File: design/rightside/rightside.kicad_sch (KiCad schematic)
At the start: 159 parts, among them IC2 XC9148G50CER-G, IC3 nRF52833-QDAA-R7, IC4 74AHCT125PW,118, IC5 MCP23018T-E_SS, IC6 XC9291B33D1R-G, J1 USB_C_Receptacle_USB2.0_16P, J2 Battery Pos, J3 Battery Neg, J4 OLED_128x32, J5 SFV12R-1STBE1HLF, J6 Conn_01x04, U2 BQ24072RGT, U3 USB6B1, U4 BQ27441-G1, U5 PEC11L-4015F-S0015, U6 PEC11L-4015F-S0015, X1 32MHz

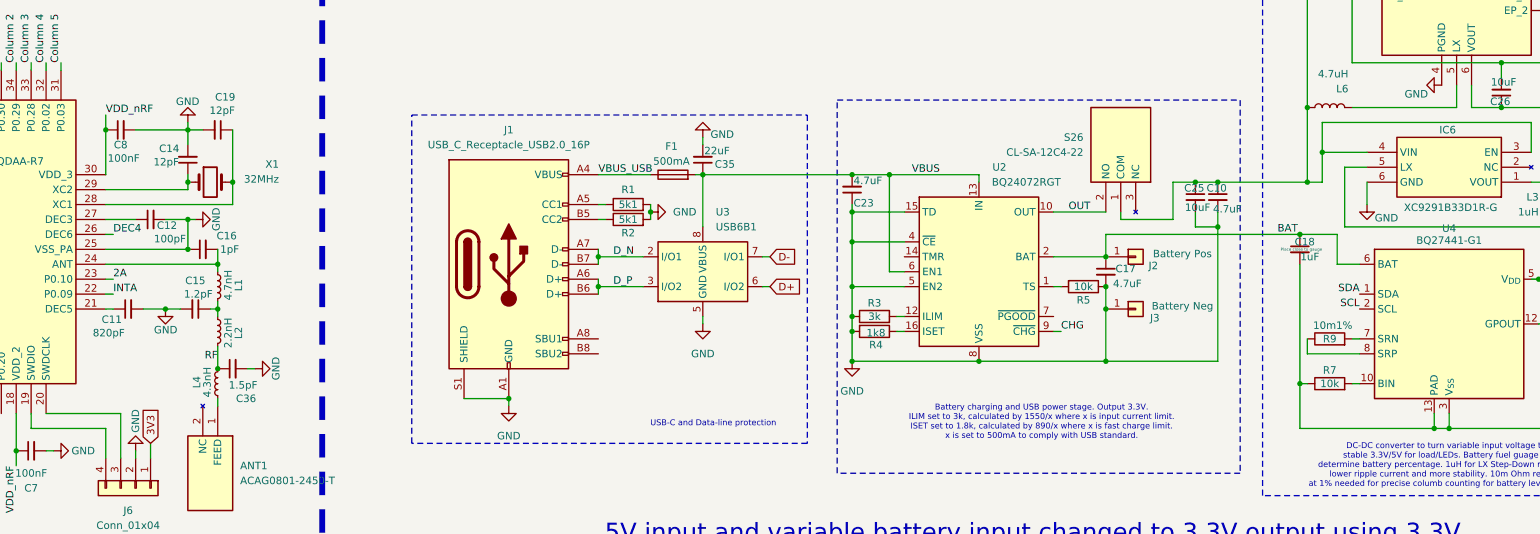
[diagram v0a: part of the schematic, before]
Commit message: correct fuel gauge and crystal
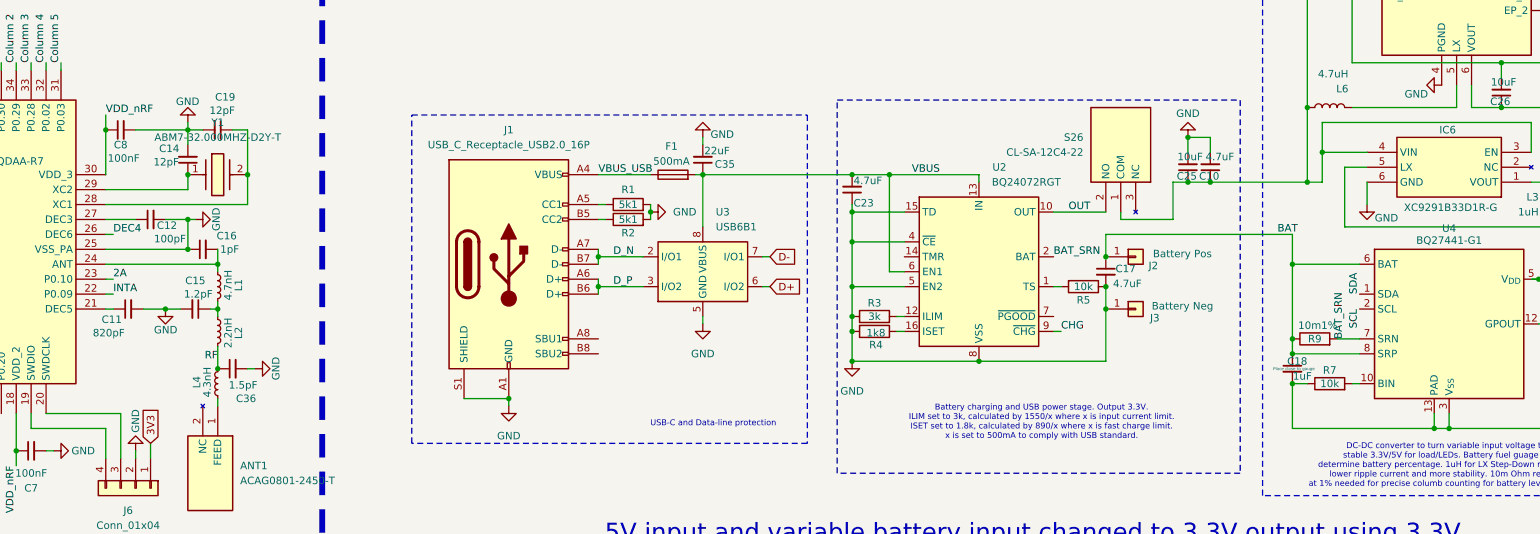
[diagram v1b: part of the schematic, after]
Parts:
- removed X1: 32MHz, Crystal:Crystal_SMD_ECS_CSM3X-2Pin_7.6x4.1mm, symbol Device:Crystal
- added Y1: ABM7-32.000MHZ-D2Y-T, ABM7, symbol SamacSys_Parts:ABM7-32.000MHZ-D2Y-T
- J6: footprint (none) -> Connector_PinHeader_2.54mm:PinHeader_1x04_P2.54mm_Horizontal
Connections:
- net BAT: now also R9.1, U4.8 (SRP); no longer U2.2 (BAT), U2.3 (BAT)
- net BAT_SRN: now reaches R9.2, U4.7 (SRN)
- net BAT_SRN: now also U2.2 (BAT), U2.3 (BAT)
- net at C14.1, IC3.29 (XC2): now also Y1.1
- net at C19.1, IC3.28 (XC1): now also Y1.2
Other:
- moved on the sheet: C10, C18, C25, R9

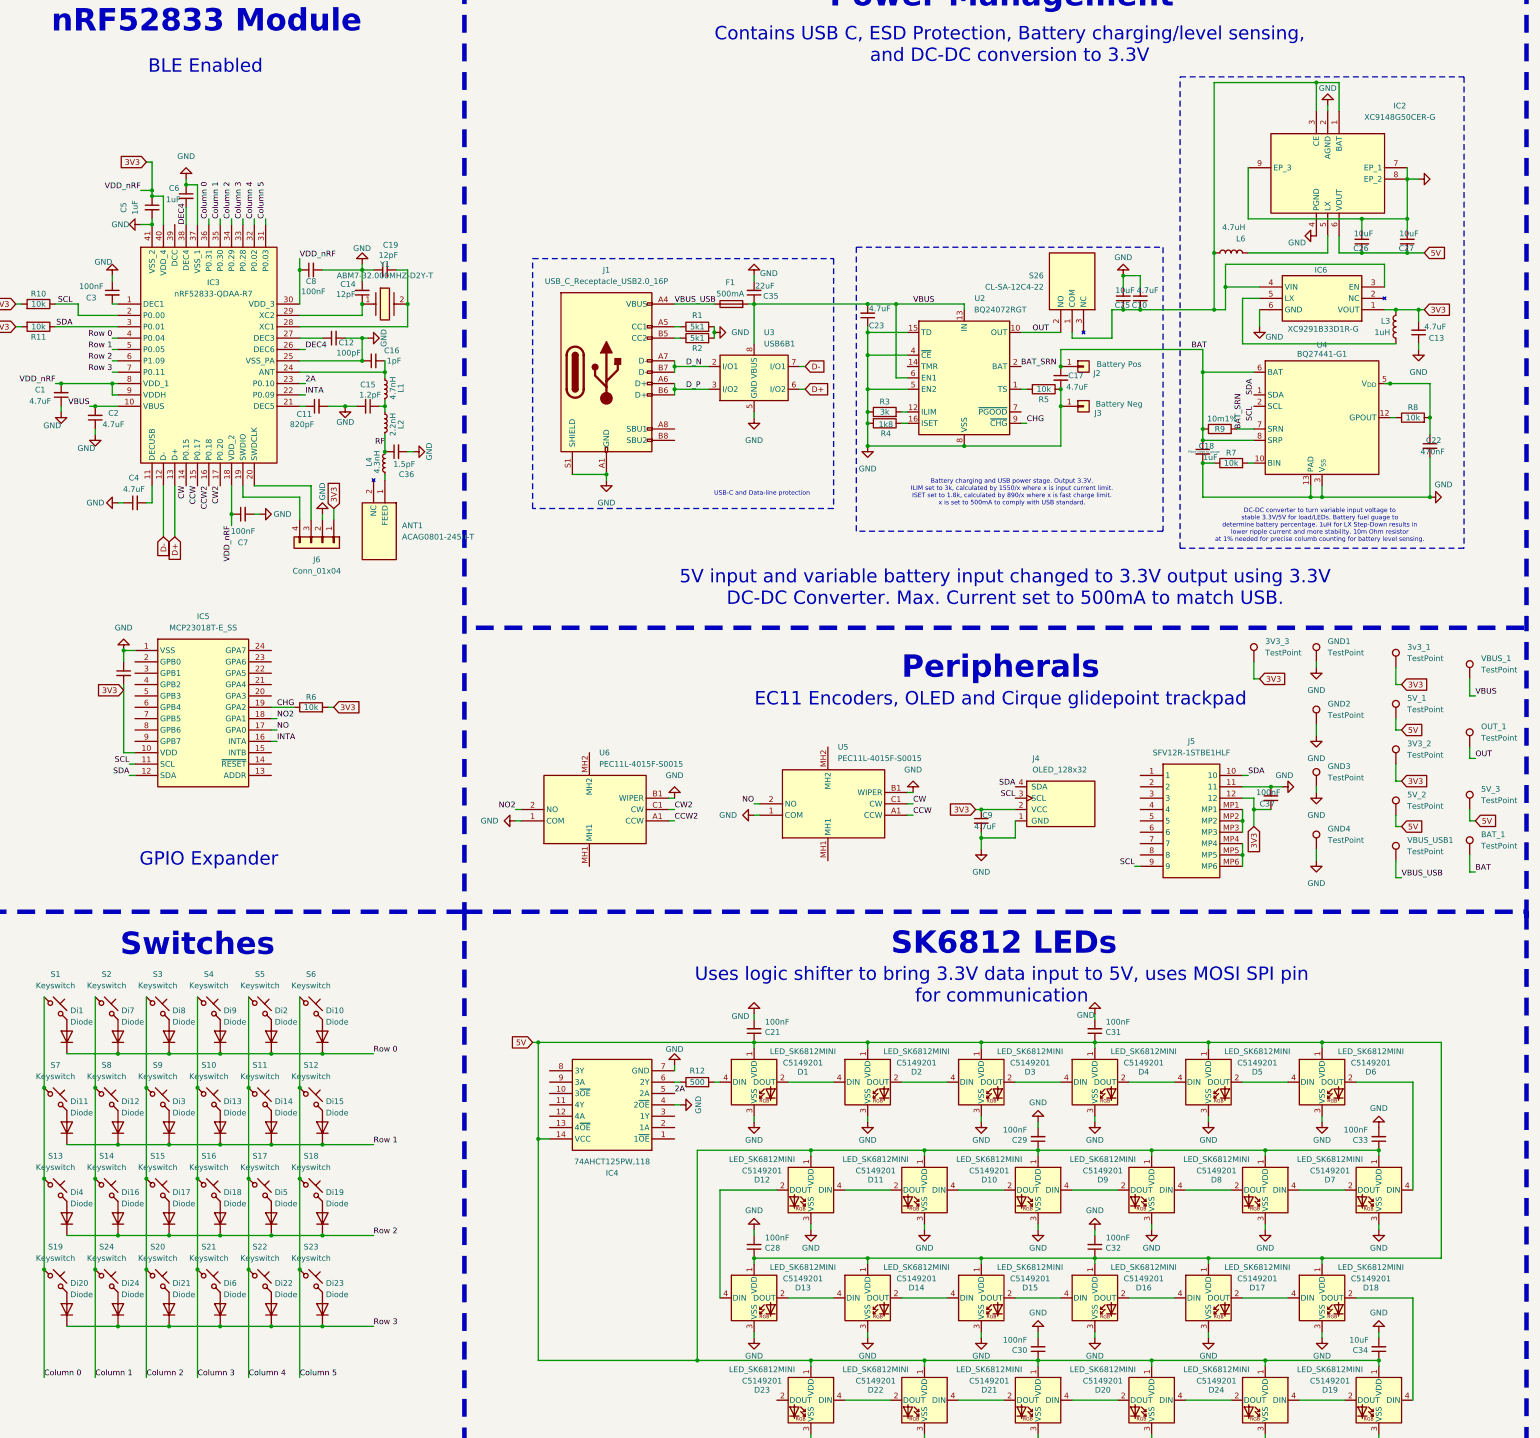
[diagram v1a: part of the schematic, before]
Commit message: prepare to reroute
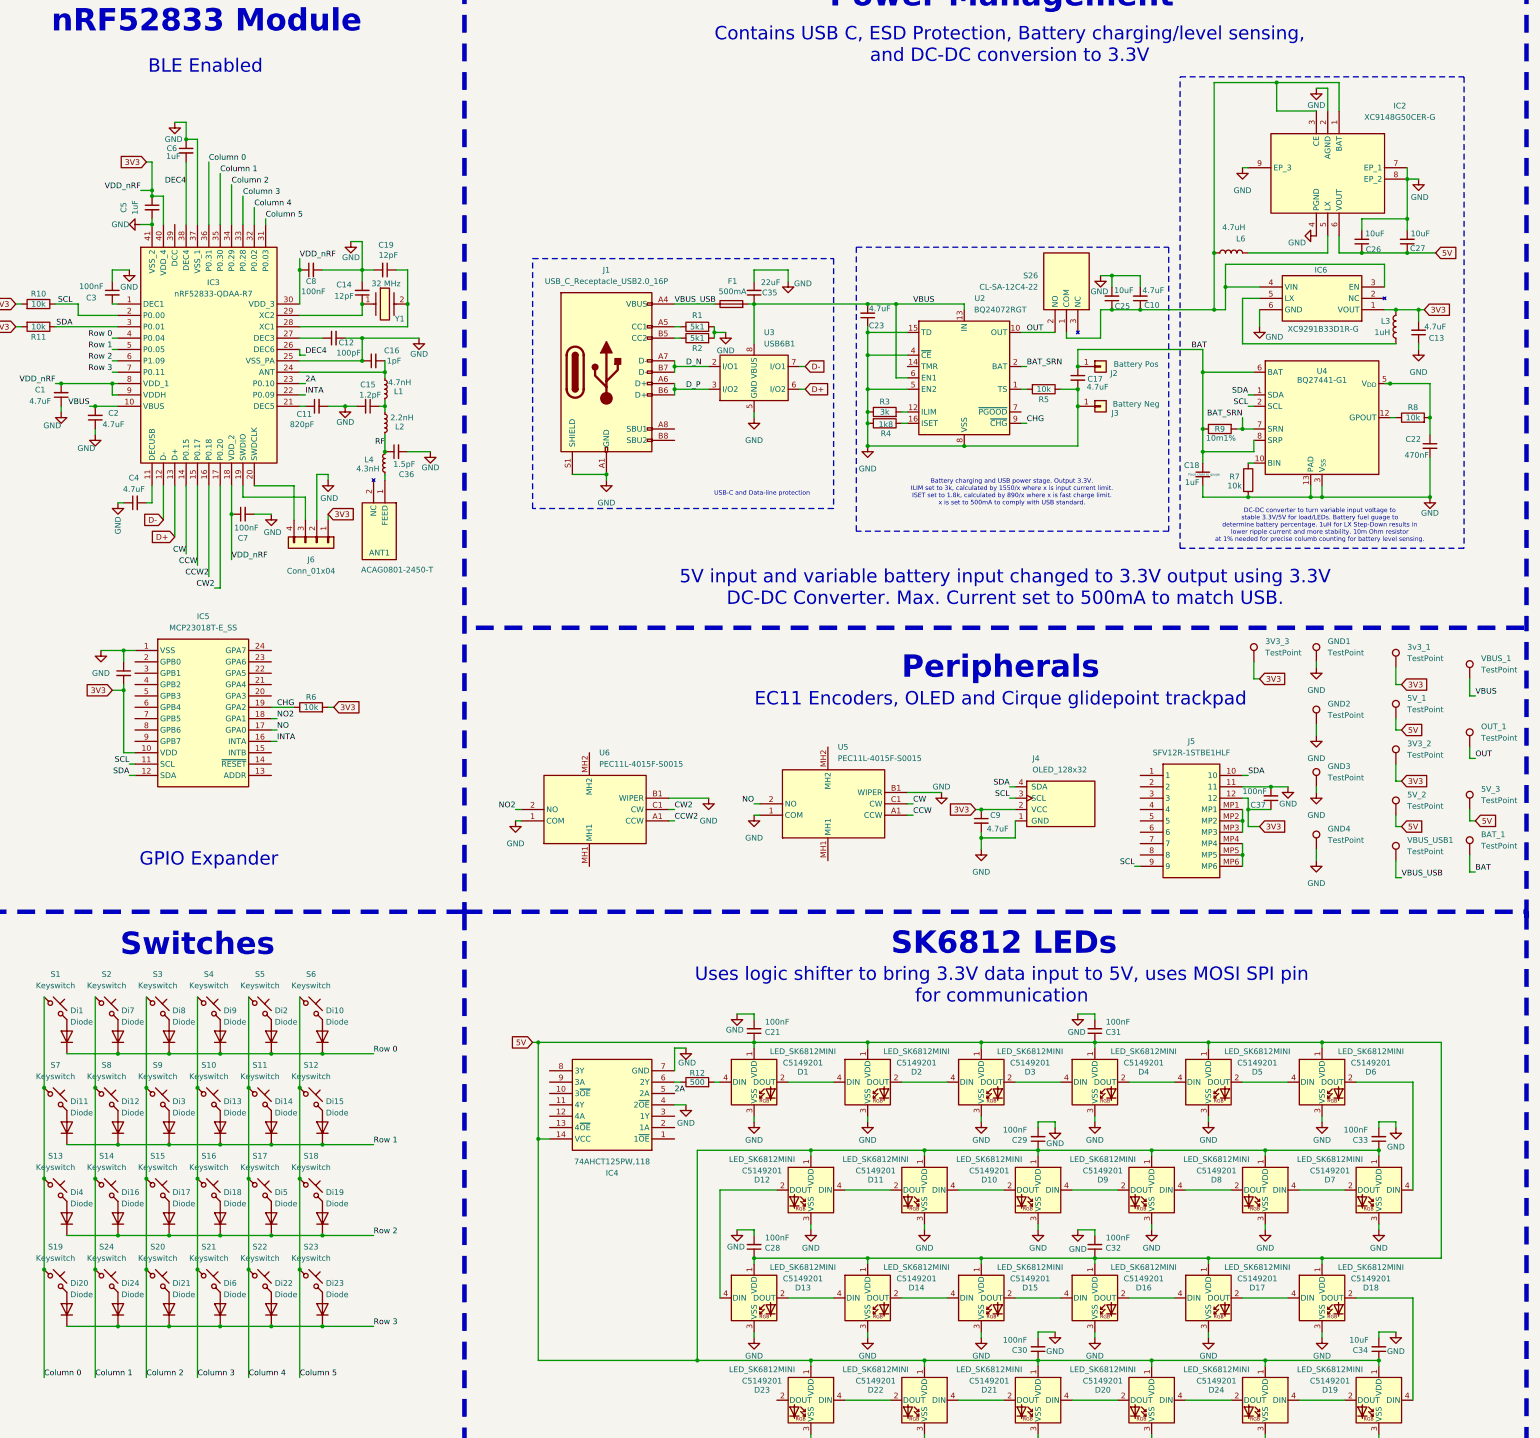
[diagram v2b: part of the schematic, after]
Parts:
- Y1: value ABM7-32.000MHZ-D2Y-T -> 32 MHz
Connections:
- net GND: now also R7.2; no longer R7.1
- net at U4.10 (BIN): now also R7.1; no longer R7.2
- net at IC3.19 (SWDIO): now also J6.3 (Pin_3); no longer J6.4 (Pin_4)
- net at IC3.20 (SWDCLK): now also J6.4 (Pin_4); no longer J6.3 (Pin_3)
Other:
- moved on the sheet: C17, C18, C25, C6, J2, J3, J6, R7, S26

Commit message: prepare to make test board
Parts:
- removed L4: 4.3nH, Inductor_SMD:L_0603_1608Metric, symbol Device:L_Small
- removed R10, R11, R6: 10k, Resistor_SMD:R_0603_1608Metric, symbol Device:R
- added C24: 4.7uF, ScottoKeebs_Components:Capacitor_0603, symbol Device:C_Small
- added C38, C39, C40: 100nF, ScottoKeebs_Components:Capacitor_0603, symbol Device:C_Small
- C35: value 22uF -> 100nF
- C36: value 1.5pF -> 100nF
- F1: value 500mA -> 600mA
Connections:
- net 3V3: now also C35.2, C36.2, C38.2, C39.2, C40.2
- net GND: now also C35.1, C36.1, C24.2, C38.1, C39.1, C40.1; no longer C35.2, C36.2
- net RF: now also ANT1.1 (FEED); no longer C36.1
- net VBUS: now also C24.1; no longer C35.1
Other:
- note added: "Stitching Capacitors"
- note added: "Test Points"
- moved on the sheet: 3V3_2, 3V3_3, 3v3_1, 5V_1, 5V_2, 5V_3, ANT1, BAT_1, C21, C28, C29, C30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

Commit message: remove old right side routing
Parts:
- removed C35, C36, C38, C39: 100nF, ScottoKeebs_Components:Capacitor_0603, symbol Device:C_Small
- removed J5: SFV12R-1STBE1HLF, SFV12R1STBE1HLF, symbol SamacSys_Parts:SFV12R-1STBE1HLF
- removed L6: 4.7uH, Inductor_SMD:L_0603_1608Metric, symbol Device:L
- removed R12: 500, Resistor_SMD:R_0603_1608Metric, symbol Device:R
- removed Y1: 32 MHz, ABM7, symbol SamacSys_Parts:ABM7-32.000MHZ-D2Y-T
- added J7: F32Q-1A7H1-11012, F32Q1A7H111012, symbol SamacSys_Parts:F32Q-1A7H1-11012
- added L4: SRN3015C-4R7M, SRN3015C4R7M, symbol SamacSys_Parts:SRN3015C-4R7M
- added R10: 3k, Resistor_SMD:R_0603_1608Metric, symbol Device:R
- added R6: 10m1%, RESC2012X41N, symbol SamacSys_Parts:TLR2ATTD10L0F
- added Y1: ECS-320-8-37B2-JTY-TR, ECS320837B2JTYTR, symbol SamacSys_Parts:ECS-320-8-37B2-JTY-TR
- C26, C27: value 10uF -> 10uF-lowESR
- R9: value 10m1% -> 10k
- renumbered 3V3_3 to 5V_4
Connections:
- net 3V3: now also R9.2, J7.12; no longer 5V_4.1
- net 5V: now also 5V_4.1
- net BAT: now also R6.1; no longer R9.1
- net BAT_SRN: now also R6.2; no longer R9.2
- net GND: now also IC4.1 (1~{OE}), IC4.10 (3~{OE}), IC4.13 (4~{OE}), IC5.13 (ADDR), J7.11, Y1.2 (GND_1), Y1.4 (GND_2)
- net SCL: now also J7.9
- net SDA: now also J7.10
- net at C10.1, C25.1, IC2.1 (BAT)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: now also L4.1
- net at D20.4 (DIN): now also D19.2 (DOUT); no longer D24.2 (DOUT)
- net at D24.4 (DIN): now also D23.2 (DOUT); no longer D19.2 (DOUT)
- net at C14.1, IC3.29 (XC2): now also Y1.1 (IN/OUT)
- net at C19.1, IC3.28 (XC1): now also Y1.3 (OUT/IN)
- net at D1.4 (DIN): now also R10.2
- net at IC2.5 (LX): now also L4.2
- net at IC5.14 (~{RESET}): now also R9.1
- net at IC4.6 (2Y): now also R10.1
- net DEC4 renamed DEC4_6
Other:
- moved on the sheet: C14, C18, C19, C22, C37, C40, D20, D21, D22, D23, D24, J6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

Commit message: restructure for right side and add correct mounting holes
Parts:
- removed OUT_1: TestPoint, TestPoint:TestPoint_Pad_D1.5mm, symbol Connector:TestPoint
- removed U4: BQ27441-G1, Package_SON:Texas_S-PDSO-N12, symbol Battery_Management:BQ27441-G1
- added 5V_5: TestPoint, TestPoint:TestPoint_Pad_D1.5mm, symbol Connector:TestPoint
- added C35, C36, C38, C39, C41, C42, C43, C45, C46: 100nF, ScottoKeebs_Components:Capacitor_0603, symbol Device:C_Small
- added C44: 10uF, ScottoKeebs_Components:Capacitor_0603, symbol Device:C_Small
- added D25, D26, D27, D28, D29, D30, D31, D32, D33, D34, D35, D36, D37, D38, D39, D40, D41, D42, D43, D44, D45, D46, D47, D48: LED_SK6812MINI, ScottoKeebs_Components:LED_SK6812MINI, symbol ScottoKeebs:LED_SK6812MINI
- added U1: BQ27441-G1, Package_SON:Texas_S-PDSO-N12, symbol Battery_Management:BQ27441-G1
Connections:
- net 3V3: no longer C40.2
- net 5V: now also C40.2, 5V_5.1, C35.1, C36.1, C38.1, C39.1, C41.1, C42.1, C43.1, C44.1, C45.1, C46.2, D25.1 (VDD), D26.1 (VDD), D27.1 (VDD), D28.1 (VDD), D29.1 (VDD), D30.1 (VDD), D31.1 (VDD), D32.1 (VDD), D33.1 (VDD), D34.1 (VDD), D35.1 (VDD), D36.1 (VDD), D37.1 (VDD), D38.1 (VDD), D39.1 (VDD), D40.1 (VDD), D41.1 (VDD), D42.1 (VDD), D43.1 (VDD), D44.1 (VDD), D45.1 (VDD), D46.1 (VDD), D47.1 (VDD), D48.1 (VDD)
- net BAT: now also U1.6 (BAT), U1.8 (SRP)
- net BAT_SRN: now also U1.7 (SRN)
- net GND: now also R7.1, U6.MH1, U6.MH2, C35.2, C36.2, C38.2, C39.2, C41.2, C42.2, C43.2, C44.2, C45.2, C46.1, D25.3 (VSS), D26.3 (VSS), D27.3 (VSS), D28.3 (VSS), D29.3 (VSS), D30.3 (VSS), D31.3 (VSS), D32.3 (VSS), D33.3 (VSS), D34.3 (VSS), D35.3 (VSS), D36.3 (VSS), D37.3 (VSS), D38.3 (VSS), D39.3 (VSS), D40.3 (VSS), D41.3 (VSS), D42.3 (VSS), D43.3 (VSS), D44.3 (VSS), D45.3 (VSS), D46.3 (VSS), D47.3 (VSS), D48.3 (VSS), U1.13 (PAD), U1.3 (V_{SS}); no longer R7.2
- net SCL: now also U1.2 (SCL)
- net SDA: now also U1.1 (SDA)
- net at R8.1: now also C22.1, U1.5 (V_{DD})
- net at R8.2: now also U1.12 (GPOUT); no longer C22.1
- net at D24.2 (DOUT): now also D25.4 (DIN)
- new net: D28.2 (DOUT), D29.4 (DIN)
- new net: D27.2 (DOUT), D28.4 (DIN)
- new net: D29.2 (DOUT), D30.4 (DIN)
- new net: D41.2 (DOUT), D42.4 (DIN)
- new net: D40.2 (DOUT), D41.4 (DIN)
- new net: D37.2 (DOUT), D38.4 (DIN)
- new net: D36.2 (DOUT), D37.4 (DIN)
- new net: D45.2 (DOUT), D46.4 (DIN)
- new net: D44.2 (DOUT), D45.4 (DIN)
- new net: D30.2 (DOUT), D31.4 (DIN)
- new net: D35.2 (DOUT), D36.4 (DIN)
- new net: D34.2 (DOUT), D35.4 (DIN)
- new net: D33.2 (DOUT), D34.4 (DIN)
- new net: D38.2 (DOUT), D39.4 (DIN)
- new net: D46.2 (DOUT), D47.4 (DIN)
- new net: D25.2 (DOUT), D26.4 (DIN)
- new net: D39.2 (DOUT), D40.4 (DIN)
- new net: R7.2, U1.10 (BIN)
- new net: D47.2 (DOUT), D48.4 (DIN)
- new net: D42.2 (DOUT), D43.4 (DIN)
- new net: D32.2 (DOUT), D33.4 (DIN)
- new net: D31.2 (DOUT), D32.4 (DIN)
- new net: D43.2 (DOUT), D44.4 (DIN)
- new net: D26.2 (DOUT), D27.4 (DIN)
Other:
- note added: "SK6803 LEDs"
- note removed: "SK6812 LEDs"
- moved on the sheet: 3V3_2, 3v3_1, 5V_1, 5V_2, 5V_3, 5V_4, ANT1, BAT_1, C1, C11, C12, C14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

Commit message: prepare to combine left and right into one pcb
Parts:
- J6: footprint Connector_PinHeader_2.54mm:PinHeader_1x04_P2.54mm_Horizontal -> Connector_PinHeader_2.54mm:PinHeader_1x04_P2.54mm_Vertical
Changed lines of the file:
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@@
 	(generator "eeschema")
 	(generator_version "8.0")
-	(paper "A2")
+	(paper "A1")
 	(junction
 		(at 96.52 100.33)
@@
 			)
 		)
-		(property "Footprint" "Connector_PinHeader_2.54mm:PinHeader_1x04_P2.54mm_Horizontal"
+		(property "Footprint" "Connector_PinHeader_2.54mm:PinHeader_1x04_P2.54mm_Vertical"
 			(at 88.9 138.43 0)
 			(effects
